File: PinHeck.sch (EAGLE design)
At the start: 328 parts, among them IC1 FT232RL-REEL, IC2 PIC32MX795F512L-80I/PT, IC3 CD74HCT244E, IC4 CD74HCT244E, IC5 ULN2803A, J1 500075-1517, J11 No Load, J2 500075-1517, J3 N/A, J6 161-3507-E, P1 TC33X-2-103E, SW1 101-0134-EV, SW2 101-0134-EV, U1 P8X32A-Q44, U10 74HCT2G04GV,125, U11 74HC165D,652, U12 74HC165D,652, U14 MC74HC08ADG, U15 MC74HC08ADG, U16 MC74HC08ADG, U17 MC74HC08ADG, U18 MC74HC08ADG, U19 MC74HC08ADG, U2 FT230XS-R, U20 TIP107, U21 TIP107, U22 TIP107, U23 TIP107, U24 TIP107, U25 TIP107, U26 TIP107, U27 TIP107, U28 TIP102, U29 TIP102, U3 74HC595D-Q100, U30 TIP102, U31 TIP102, U32 TIP102, U33 TIP102, U34 TIP102, U35 TIP102, U36 WS2801, U37 TIP102, U38 WS2801, U39 LM2937IMP-3.3/NOPB, U4 24LC1025-I/P, U40 TIP102, U41 TIP102, U42 TIP102, U43 TIP102, U44 TIP102, U45 TIP102, U46 TIP102, U47 TIP102, U48 TIP102, U49 TIP102, U5 74HC595D-Q100, U50 TIP102, U51 TIP102, U52 CD74HC123M96, U6 TIP102, U7 TIP102, U8 TIP102, U9 TIP102, X1 FQ7050B-8.000, X2 ECS-65-20-4X

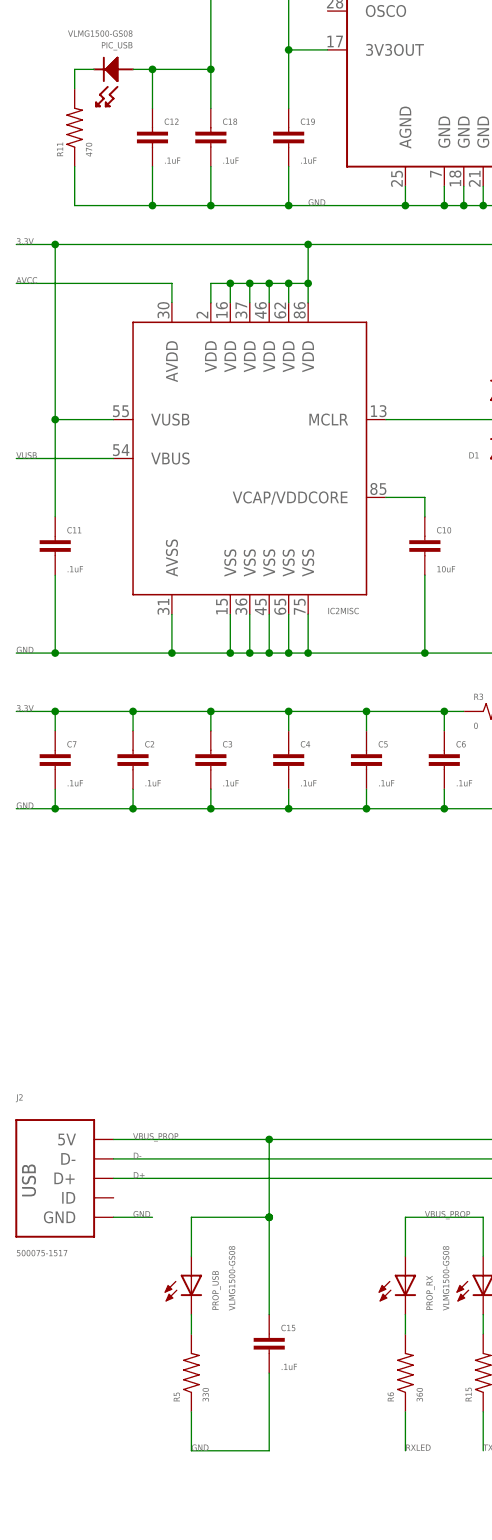
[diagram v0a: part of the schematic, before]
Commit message: Changed some resistors to there correct number.
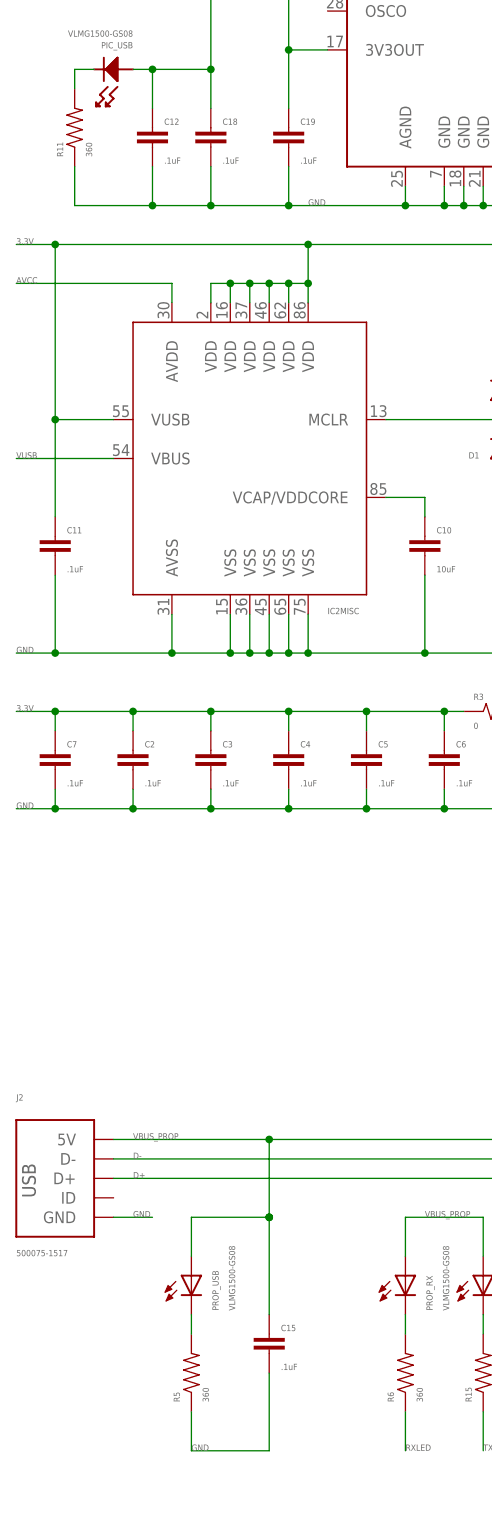
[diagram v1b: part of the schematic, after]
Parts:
- R11: value 470 -> 360
- R5: value 330 -> 360
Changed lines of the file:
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@@
 <grid distance="0.1" unitdist="inch" unit="inch" style="lines" multiple="1" display="no" altdistance="0.01" altunitdist="inch" altunit="inch"/>
 <layers>
-<layer number="1" name="Top" color="4" fill="1" visible="yes" active="no"/>
-<layer number="2" name="Route2" color="1" fill="3" visible="yes" active="no"/>
-<layer number="3" name="Route3" color="4" fill="3" visible="yes" active="no"/>
-<layer number="4" name="Route4" color="1" fill="4" visible="yes" active="no"/>
-<layer number="5" name="Route5" color="4" fill="4" visible="yes" active="no"/>
-<layer number="6" name="Route6" color="1" fill="8" visible="yes" active="no"/>
-<layer number="7" name="Route7" color="4" fill="8" visible="yes" active="no"/>
-<layer number="8" name="Route8" color="1" fill="2" visible="yes" active="no"/>
-<layer number="9" name="Route9" color="4" fill="2" visible="yes" active="no"/>
-<layer number="10" name="Route10" color="1" fill="7" visible="yes" active="no"/>
-<layer number="11" name="Route11" color="4" fill="7" visible="yes" active="no"/>
-<layer number="12" name="Route12" color="1" fill="5" visible="yes" active="no"/>
-<layer number="13" name="Route13" color="4" fill="5" visible="yes" active="no"/>
-<layer number="14" name="Route14" color="1" fill="6" visible="yes" active="no"/>
-<layer number="15" name="Route15" color="4" fill="6" visible="yes" active="no"/>
-<layer number="16" name="Bottom" color="1" fill="1" visible="yes" active="no"/>
-<layer number="17" name="Pads" color="2" fill="1" visible="yes" active="no"/>
-<layer number="18" name="Vias" color="2" fill="1" visible="yes" active="no"/>
-<layer number="19" name="Unrouted" color="6" fill="1" visible="yes" active="no"/>
-<layer number="20" name="Dimension" color="15" fill="1" visible="yes" active="no"/>
-<layer number="21" name="tPlace" color="7" fill="1" visible="yes" active="no"/>
-<layer number="22" name="bPlace" color="7" fill="1" visible="yes" active="no"/>
-<layer number="23" name="tOrigins" color="15" fill="1" visible="yes" active="no"/>
-<layer number="24" name="bOrigins" color="15" fill="1" visible="yes" active="no"/>
-<layer number="25" name="tNames" color="7" fill="1" visible="yes" active="no"/>
-<layer number="26" name="bNames" color="7" fill="1" visible="yes" active="no"/>
-<layer number="27" name="tValues" color="7" fill="1" visible="yes" active="no"/>
-<layer number="28" name="bValues" color="7" fill="1" visible="yes" active="no"/>
+<layer number="1" name="Top" color="4" fill="1" visible="no" active="no"/>
+<layer number="2" name="Route2" color="1" fill="3" visible="no" active="no"/>
+<layer number="3" name="Route3" color="4" fill="3" visible="no" active="no"/>
+<layer number="4" name="Route4" color="1" fill="4" visible="no" active="no"/>
+<layer number="5" name="Route5" color="4" fill="4" visible="no" active="no"/>
+<layer number="6" name="Route6" color="1" fill="8" visible="no" active="no"/>
+<layer number="7" name="Route7" color="4" fill="8" visible="no" active="no"/>
+<layer number="8" name="Route8" color="1" fill="2" visible="no" active="no"/>
+<layer number="9" name="Route9" color="4" fill="2" visible="no" active="no"/>
+<layer number="10" name="Route10" color="1" fill="7" visible="no" active="no"/>
+<layer number="11" name="Route11" color="4" fill="7" visible="no" active="no"/>
+<layer number="12" name="Route12" color="1" fill="5" visible="no" active="no"/>
+<layer number="13" name="Route13" color="4" fill="5" visible="no" active="no"/>
+<layer number="14" name="Route14" color="1" fill="6" visible="no" active="no"/>
+<layer number="15" name="Route15" color="4" fill="6" visible="no" active="no"/>
+<layer number="16" name="Bottom" color="1" fill="1" visible="no" active="no"/>
+<layer number="17" name="Pads" color="2" fill="1" visible="no" active="no"/>
+<layer number="18" name="Vias" color="2" fill="1" visible="no" active="no"/>
+<layer number="19" name="Unrouted" color="6" fill="1" visible="no" active="no"/>
+<layer number="20" name="Dimension" color="15" fill="1" visible="no" active="no"/>
+<layer number="21" name="tPlace" color="7" fill="1" visible="no" active="no"/>
+<layer number="22" name="bPlace" color="7" fill="1" visible="no" active="no"/>
+<layer number="23" name="tOrigins" color="15" fill="1" visible="no" active="no"/>
+<layer number="24" name="bOrigins" color="15" fill="1" visible="no" active="no"/>
+<layer number="25" name="tNames" color="7" fill="1" visible="no" active="no"/>
+<layer number="26" name="bNames" color="7" fill="1" visible="no" active="no"/>
+<layer number="27" name="tValues" color="7" fill="1" visible="no" active="no"/>
+<layer number="28" name="bValues" color="7" fill="1" visible="no" active="no"/>
 <layer number="29" name="tStop" color="7" fill="3" visible="no" active="no"/>
 <layer number="30" name="bStop" color="7" fill="6" visible="no" active="no"/>
@@
 <layer number="35" name="tGlue" color="7" fill="4" visible="no" active="no"/>
 <layer number="36" name="bGlue" color="7" fill="5" visible="no" active="no"/>
-<layer number="37" name="tTest" color="7" fill="1" visible="yes" active="no"/>
-<layer number="38" name="bTest" color="7" fill="1" visible="yes" active="no"/>
+<layer number="37" name="tTest" color="7" fill="1" visible="no" active="no"/>
+<layer number="38" name="bTest" color="7" fill="1" visible="no" active="no"/>
 <layer number="39" name="tKeepout" color="4" fill="11" visible="no" active="no"/>
 <layer number="40" name="bKeepout" color="1" fill="11" visible="no" active="no"/>
@@
 <layer number="44" name="Drills" color="7" fill="1" visible="no" active="no"/>
 <layer number="45" name="Holes" color="7" fill="1" visible="no" active="no"/>
-<layer number="46" name="Milling" color="3" fill="1" visible="yes" active="no"/>
-<layer number="47" name="Measures" color="7" fill="1" visible="yes" active="no"/>
-<layer number="48" name="Document" color="7" fill="1" visible="yes" active="no"/>
-<layer number="49" name="Reference" color="7" fill="1" visible="yes" active="no"/>
-<layer number="50" name="dxf" color="7" fill="1" visible="yes" active="no"/>
-<layer number="51" name="tDocu" color="7" fill="1" visible="yes" active="no"/>
-<layer number="52" name="bDocu" color="7" fill="1" visible="yes" active="no"/>
-<layer number="53" name="tGND_GNDA" color="7" fill="9" visible="yes" active="no"/>
-<layer number="54" name="bGND_GNDA" color="1" fill="9" visible="yes" active="no"/>
-<layer number="56" name="wert" color="7" fill="1" visible="yes" active="no"/>
+<layer number="46" name="Milling" color="3" fill="1" visible="no" active="no"/>
+<layer number="47" name="Measures" color="7" fill="1" visible="no" active="no"/>
+<layer number="48" name="Document" color="7" fill="1" visible="no" active="no"/>
+<layer number="49" name="Reference" color="7" fill="1" visible="no" active="no"/>
+<layer number="50" name="dxf" color="7" fill="1" visible="no" active="no"/>
+<layer number="51" name="tDocu" color="7" fill="1" visible="no" active="no"/>
+<layer number="52" name="bDocu" color="7" fill="1" visible="no" active="no"/>
+<layer number="53" name="tGND_GNDA" color="7" fill="9" visible="no" active="no"/>
+<layer number="54" name="bGND_GNDA" color="1" fill="9" visible="no" active="no"/>
+<layer number="56" name="wert" color="7" fill="1" visible="no" active="no"/>
 <layer number="91" name="Nets" color="2" fill="1" visible="yes" active="yes"/>
 <layer number="92" name="Busses" color="1" fill="1" visible="yes" active="yes"/>
@@
 <part name="C12" library="PP_Passives" deviceset="CAPACITOR_NON_POLAR" device="0805" value=".1uF"/>
 <part name="PIC_USB" library="PP_LED" deviceset="LED_SINGLE" device="0402" value="VLMG1500-GS08"/>
-<part name="R11" library="PP_Passives" deviceset="RESISTOR" device="0805" value="470"/>
+<part name="R11" library="PP_Passives" deviceset="RESISTOR" device="0805" value="360"/>
 <part name="C2" library="PP_Passives" deviceset="CAPACITOR_NON_POLAR" device="0805" value=".1uF"/>
 <part name="C3" library="PP_Passives" deviceset="CAPACITOR_NON_POLAR" device="0805" value=".1uF"/>
@@
 <part name="C15" library="PP_Passives" deviceset="CAPACITOR_NON_POLAR" device="0805" value=".1uF"/>
 <part name="C16" library="PP_Passives" deviceset="CAPACITOR_NON_POLAR" device="0805" value=".1uF"/>
-<part name="R5" library="PP_Passives" deviceset="RESISTOR" device="0805" value="330"/>
+<part name="R5" library="PP_Passives" deviceset="RESISTOR" device="0805" value="360"/>
 <part name="PROP_RX" library="led" deviceset="LED" device="SML0603" value="VLMG1500-GS08"/>
 <part name="PROP_TX" library="led" deviceset="LED" device="SML0603" value="VLMG1500-GS08"/>

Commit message: Changed LEDs to 0805 package.
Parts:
- removed WATCHDOG: VLMG1500-GS08, led:LEDSML0603
- added WD: LG R971-KN-1, PP_LED:LED_SINGLE0805
- PIC_RX, PIC_TX, PIC_USB: value VLMG1500-GS08 -> LG R971-KN-1; device PP_LED:LED_SINGLE0402 -> PP_LED:LED_SINGLE0805
- PROP_ACT, PROP_RX, PROP_TX, PROP_USB, PSU_PWR: value VLMG1500-GS08 -> LG R971-KN-1; device led:LEDSML0603 -> PP_LED:LED_SINGLE0805
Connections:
- net 3.3V: now also PSU_PWR.ANODE; no longer PSU_PWR.A
- net D1: now also PROP_USB.CATHODE; no longer PROP_USB.C
- net D2: now also PROP_RX.CATHODE; no longer PROP_RX.C
- net D3: now also PROP_TX.CATHODE; no longer PROP_TX.C
- net N$3: now also PROP_ACT.CATHODE; no longer PROP_ACT.C
- net N$50: now also WD.CATHODE; no longer WATCHDOG.C
- net N$51: now also PSU_PWR.CATHODE; no longer PSU_PWR.C
- net P27: now also PROP_ACT.ANODE; no longer PROP_ACT.A
- net VBUS_PROP: now also PROP_RX.ANODE, PROP_TX.ANODE, PROP_USB.ANODE; no longer PROP_RX.A, PROP_TX.A, PROP_USB.A
- net WATCHDOG: now also WD.ANODE; no longer WATCHDOG.A

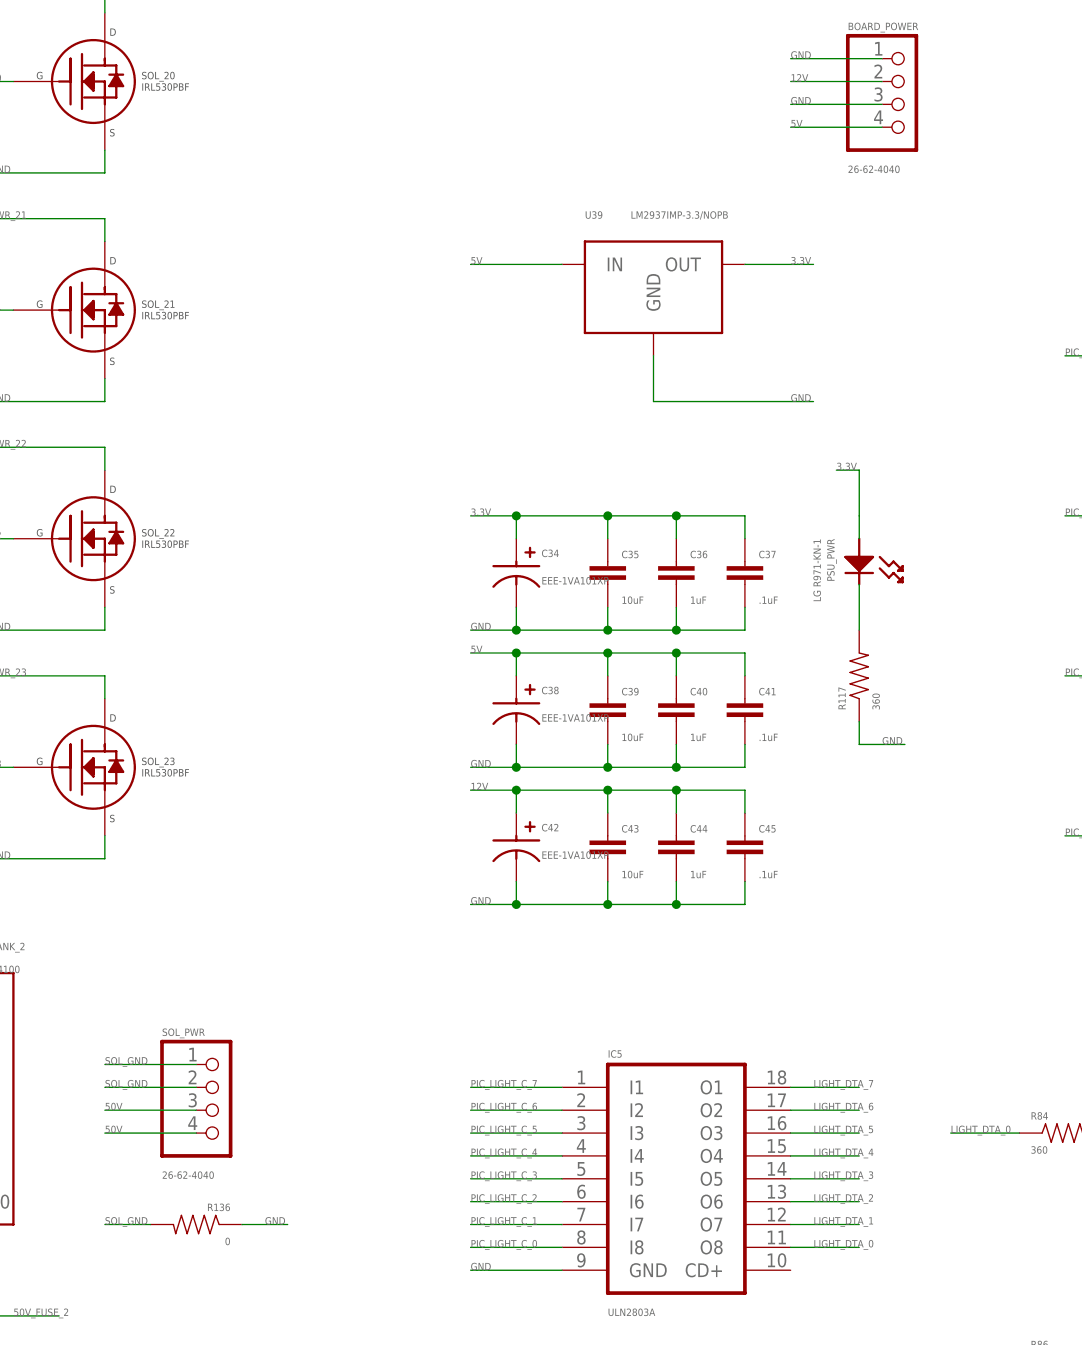
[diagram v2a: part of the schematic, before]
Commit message: Updated Bill of Materials.
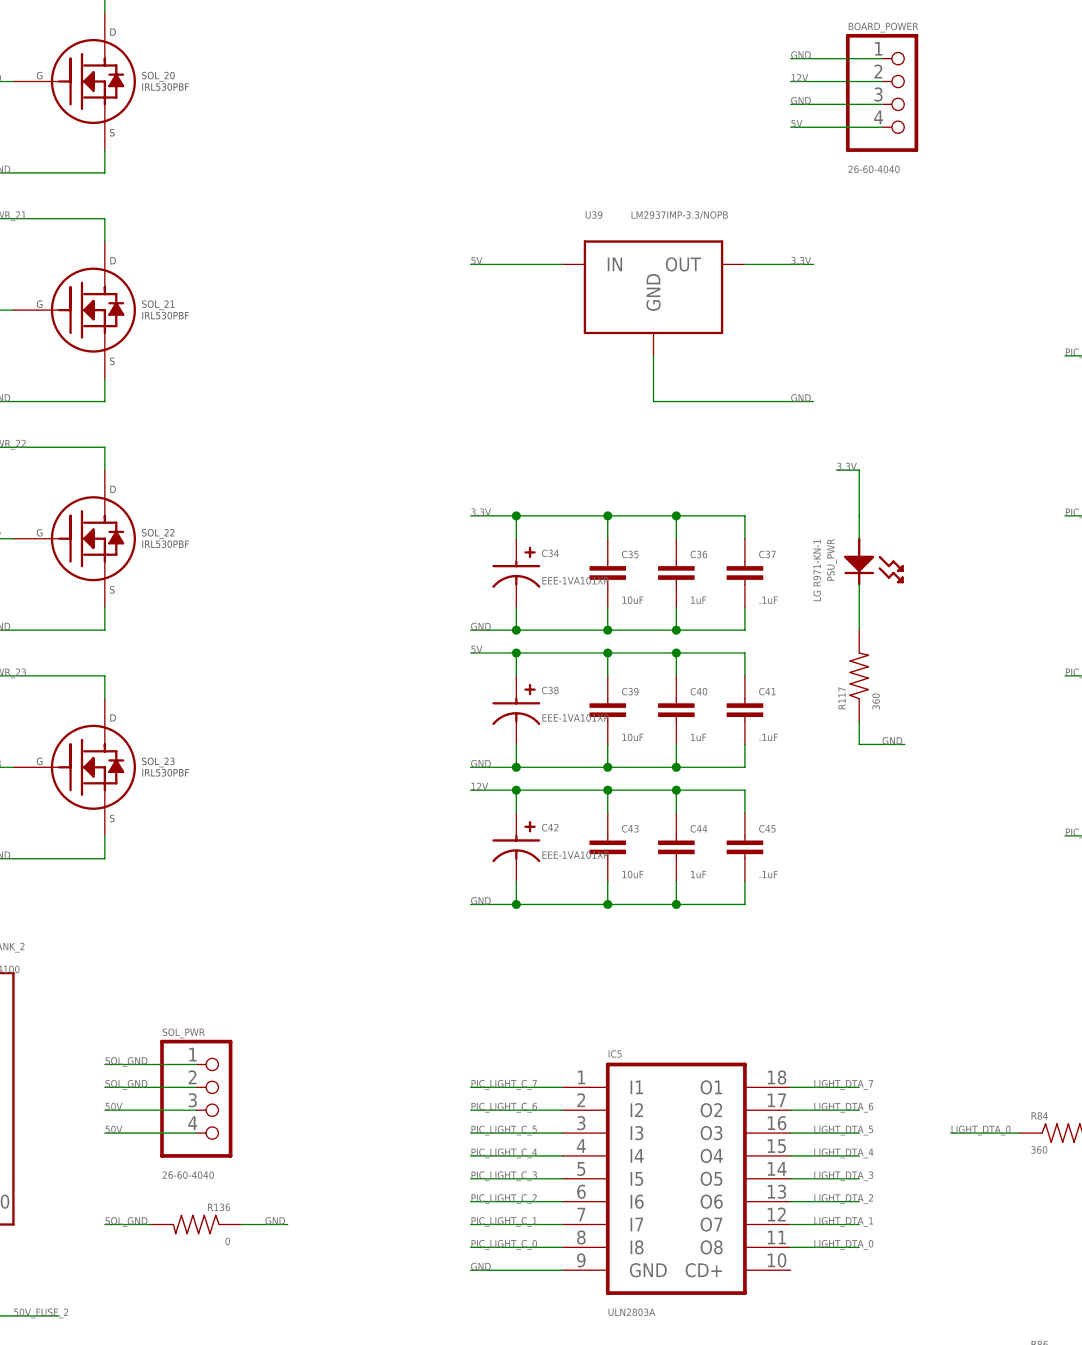
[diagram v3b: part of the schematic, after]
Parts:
- BOARD_POWER, SOL_PWR: value 26-62-4040 -> 26-60-4040
- C10: device PP_Passives:CAPACITOR_NON_POLAR0805 -> PP_Passives:CAPACITOR_NON_POLAR1206
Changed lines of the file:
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@@
 <?xml version="1.0" encoding="utf-8"?>
 <!DOCTYPE eagle SYSTEM "eagle.dtd">
-<eagle version="6.3">
+<eagle version="6.5.0">
 <drawing>
 <settings>
@@
 <part name="C9" library="PP_Passives" deviceset="CAPACITOR_NON_POLAR" device="0805" value=".1uF"/>
 <part name="C11" library="PP_Passives" deviceset="CAPACITOR_NON_POLAR" device="0805" value=".1uF"/>
-<part name="C10" library="PP_Passives" deviceset="CAPACITOR_NON_POLAR" device="0805" value="10uF"/>
+<part name="C10" library="PP_Passives" deviceset="CAPACITOR_NON_POLAR" device="1206" value="10uF"/>
 <part name="R12" library="PP_Passives" deviceset="RESISTOR" device="0805" value="50"/>
 <part name="R8" library="PP_Passives" deviceset="RESISTOR" device="0805" value="200"/>
@@
 <part name="F2" library="PP_Passives" deviceset="PTC_FUSE" device="4245K" value="4245K"/>
 <part name="F3" library="PP_Passives" deviceset="PTC_FUSE" device="4245K" value="4245K"/>
-<part name="SOL_PWR" library="PP_Connectors" deviceset="PH_1X04" device="KK_4" value="26-62-4040"/>
+<part name="SOL_PWR" library="PP_Connectors" deviceset="PH_1X04" device="KK_4" value="26-60-4040"/>
 <part name="R51" library="PP_Passives" deviceset="RESISTOR" device="0805" value="10K"/>
 <part name="R52" library="PP_Passives" deviceset="RESISTOR" device="0805" value="10K"/>
@@
 <part name="C46" library="PP_Passives" deviceset="CAPACITOR_NON_POLAR" device="0805" value=".1uF"/>
 <part name="C47" library="PP_Passives" deviceset="CAPACITOR_NON_POLAR" device="0805" value=".1uF"/>
-<part name="BOARD_POWER" library="PP_Connectors" deviceset="PH_1X04" device="KK_4" value="26-62-4040"/>
+<part name="BOARD_POWER" library="PP_Connectors" deviceset="PH_1X04" device="KK_4" value="26-60-4040"/>
 <part name="U39" library="PP_PowerIC" deviceset="FIXED_VOLTAGE_REG" device="SOT-223" value="LM2937IMP-3.3/NOPB"/>
 <part name="C48" library="PP_Passives" deviceset="CAPACITOR_NON_POLAR" device="0805" value="1uF"/>
